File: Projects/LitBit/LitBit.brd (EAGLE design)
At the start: 160 x 100 mm, 1 part

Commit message: almost milestoneeeE??
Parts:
- removed U$1: ATMEGA32U4-AU, adafruit:TQFP44
- added C1, C18, C19: 10uF, SCADA_CUSTOM_LIBRARY:0603-POLAR
- added C10, C11, C15: 100nF, SCADA_CUSTOM_LIBRARY:0603-CUSTOM
- added C12, C13, C16, C17, C7, C8: 12p, SCADA_CUSTOM_LIBRARY:0603-CUSTOM
- added C14, C26: 1uF, SCADA_CUSTOM_LIBRARY:0603-CUSTOM
- added C2, C25, C3: 4.7uF, SCADA_CUSTOM_LIBRARY:0603-CUSTOM
- added C20: 1 nF, SCADA_CUSTOM_LIBRARY:0603-CUSTOM
- added C21: 1.2 pF, SCADA_CUSTOM_LIBRARY:0603-CUSTOM
- added C22: 1.5 pF, SCADA_CUSTOM_LIBRARY:0603-CUSTOM
- added C23: 1.8 pF, SCADA_CUSTOM_LIBRARY:0603-CUSTOM
- added C24: 2.2 nF, SCADA_CUSTOM_LIBRARY:0603-CUSTOM
- added C27, C4, C5, C6: 100n, SCADA_CUSTOM_LIBRARY:0603-CUSTOM
- added C28, C29: 22p, SCADA_CUSTOM_LIBRARY:0603-CUSTOM
- added C9: 33nF, SCADA_CUSTOM_LIBRARY:0603-CUSTOM
- added D1: Green, Wurth_Elektronik_Optoelectronics_rev18a:WL-SMCW_0603
- added FB1, FB2: (no value), SCADA_CUSTOM_LIBRARY:0603-CUSTOM
- added ISP1: AVRISP-6, adafruit:AVRISP
- added JMP1: 0R-JUMPA, SCADA_CUSTOM_LIBRARY:AOR-JMP-0603
- added JP1, JP10, JP2, JP3, JP4, JP5, JP6, JP7, JP9: (no value), microbuilder:JUMPER2
- added JP11: BLE_SPI, jumper:JP3Q
- added JP12: Display, adafruit:1X06
- added JP8: I2c, pinhead:1X02
- added L1: 15 nH, SCADA_CUSTOM_LIBRARY:0603-CUSTOM
- added L2: 10 uH, SCADA_CUSTOM_LIBRARY:0805-CUSTOM
- added L3: 5.6 nH, SCADA_CUSTOM_LIBRARY:0603-CUSTOM
- added L4: 8.2 nH, SCADA_CUSTOM_LIBRARY:0603-CUSTOM
- added L5: 3.9 nH, SCADA_CUSTOM_LIBRARY:0603-CUSTOM
- added R1: 22k, SCADA_CUSTOM_LIBRARY:0603-CUSTOM
- added R2, R7: 0R, SCADA_CUSTOM_LIBRARY:0603-CUSTOM
- added R3: 47k, SCADA_CUSTOM_LIBRARY:0603-CUSTOM
- added R4: 330, SCADA_CUSTOM_LIBRARY:0603-CUSTOM
- added R5, R6, R8: 10k, SCADA_CUSTOM_LIBRARY:0603-CUSTOM
- added TP1: TEST_POINT_40MIL_DIA, SCADA_CUSTOM_LIBRARY:TEST_POINT_40MIL_DIA
- added U$28: (no value), microbuilder:ANT_PCB_2.4GHZ_NRF8001_1.6MM_1OZ
- added U1: 24FC1025, SCADA_CUSTOM_LIBRARY:8-SOIC_HAND_SOLDER
- added U2: MCP7490N, SCADA_CUSTOM_LIBRARY:8-SOIC_HAND_SOLDER
- added U3: ADXL345, SCADA_CUSTOM_LIBRARY:LGA-14
- added U4: ATMEGA32U4-AU, SCADA_CUSTOM_LIBRARY:TQFP44
- added U5: S-1335J33-M5T1U3, SCADA_CUSTOM_LIBRARY:SOT23-5_HAND_SOLDER
- added U6: nRF8001, microbuilder:QFN32_5MM
- added U7: MCP73831, SCADA_CUSTOM_LIBRARY:SOT23-5_HAND_SOLDER
- added USB1: ZX62-B-5PA, Seeed-Connector:MICRO-USB5+6P-SMD-0.65-AB
- added Y1: 16.0000 MHz, SCADA_CUSTOM_LIBRARY:4-SMD
- added Y2, Y3: 32.7680 kHz, SCADA_CUSTOM_LIBRARY:4-SOJ
- added Y4: 8.0000 MHz, adafruit:HC49UP
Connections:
- new net 3.3V: C19.1, FB1.1, ISP1.2, JMP1.3, JP2.2, JP3.2, JP5.2, JP9.2, R5.2, R6.2, R7.1, U5.5
- new net ACTIVE: U6.6
- new net AGND: R2.1, U3.2, U3.4, U3.5
- new net AVCC: JP10.2, JP7.2, R7.2
- new net D+: U4.4, USB1.3
- new net D-: U4.3, USB1.2
- new net MFP: R8.1, U2.7
- new net MISO: ISP1.1, JP11.5
- new net MISO_3V3: JP11.6, U6.14
- new net MOSI: ISP1.4, JP11.3, U4.10
- new net MOSI_3V3: JP11.4, U6.13
- new net N$1: C7.2, U2.1, Y3.P4
- new net N$10: L1.1, L2.2
- new net N$11: L2.1, U6.32
- new net N$12: C16.1, U6.28, Y1.P3
- new net N$13: JMP1.2, U5.4
- new net N$14: C18.1, JP1.1, U5.1, U5.3
- new net N$15: C4.1, JP2.1, R8.2, U2.8
- new net N$16: C3.1, JP4.1, U7.3
- new net N$17: C26.1, C5.1, JP3.1, U1.3, U1.8
- new net N$18: C17.1, U6.27, Y1.P1
- new net N$19: C23.2, L5.2
- new net N$2: C8.2, U2.2, Y3.P1
- new net N$20: L4.2, L5.1, U6.22
- new net N$21: L3.1, L4.1, U6.21
- new net N$22: R1.1, U6.25
- new net N$23: C24.1, L3.2, U6.20
- new net N$24: C21.1, C22.1, C23.1, U$28.FEED
- new net N$25: D1.1, R4.2
- new net N$26: R3.2, U7.5
- new net N$27: R4.1, U7.1
- new net N$28: C25.1, JP9.1, U4.14, U4.34
- new net N$29: C28.2, U4.16, Y4.1
- new net N$3: C10.1, U6.2
- new net N$30: C29.2, U4.17, Y4.2
- new net N$32: FB2.2, JP10.1
- new net N$33: C27.1, FB2.1, U4.24, U4.44
- new net N$34: TP1.TP$1, U4.42
- new net N$4: C9.1, U6.3
- new net N$5: C12.2, U6.4, Y2.P4
- new net N$6: C13.2, U6.5, Y2.P1
- new net N$7: C2.1, D1.2, JP6.1, U7.4
- new net N$8: C1.1, C15.1, JP5.1, U6.1, U6.9
- new net N$9: C6.2, JP7.1, U3.6
- new net RDYN: U6.16
- new net REQN_3V3: U6.12
- new net RST: ISP1.5, U4.13
- new net RST_NRF: U6.19
- new net SCK: ISP1.3, JP11.1, U4.9
- new net SCK_3V3: JP11.2, U6.11
- new net SCL: JP8.2, R5.1, U1.6, U2.6, U3.14, U4.18
- new net SDA: JP8.1, R6.1, U1.5, U2.5, U3.13, U4.19
- new net SHIELD: USB1.5, USB1.P1, USB1.P2, USB1.P3, USB1.P4, USB1.P5, USB1.P6
- new net VDDA: C11.1, C14.1, C20.1, FB1.2, L1.2, U6.24, U6.26, U6.29
- new net V_BATT: JP1.2, JP4.2
- new net V_USB: JP6.2, U4.7, USB1.1
- net GND: now also C1.2, C10.2, C11.2, C12.1, C13.1, C14.2, C15.2, C16.2, C17.2, C18.2, C19.2, C2.2, C20.2, C21.2, C22.2, C24.2, C25.2, C26.2, C27.2, C28.1, C29.1, C3.2, C4.2, C5.2, C6.1, C7.1, C8.1, C9.2, ISP1.6, JMP1.1, R1.2, R2.2, R3.1, U1.1, U1.2, U1.4, U1.7, U2.3, U2.4, U4.15, U4.23, U4.35, U4.43, U4.5, U5.2, U6.17, U6.18, U6.23, U6.30, U6.31, U6.33, U6.8, U7.2; no longer U$1.15, U$1.23, U$1.35, U$1.43
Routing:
- added copper zone on layer 1, net GND

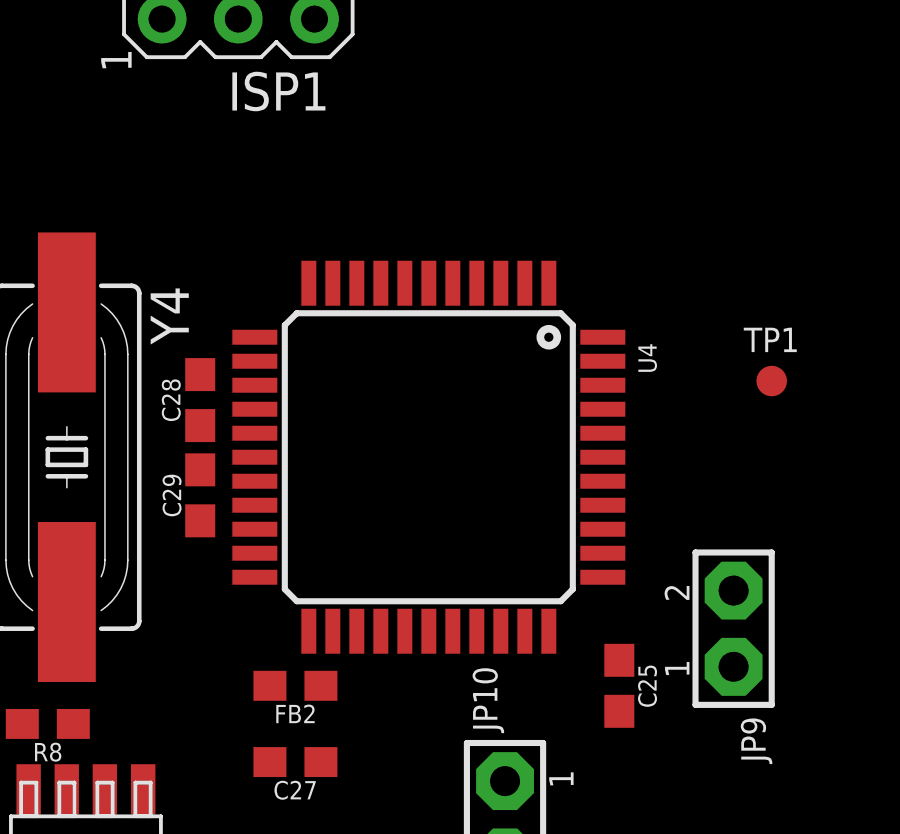
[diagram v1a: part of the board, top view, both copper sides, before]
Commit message: Change processor package to VQFN to save space.
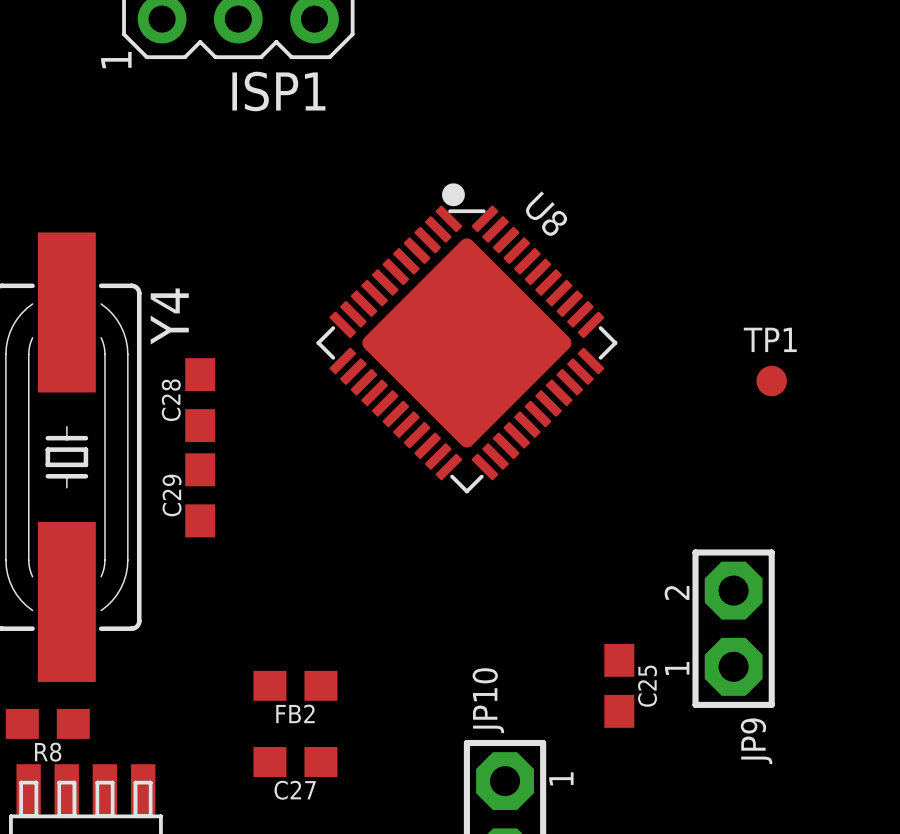
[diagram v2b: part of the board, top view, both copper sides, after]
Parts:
- removed U4: ATMEGA32U4-AU, SCADA_CUSTOM_LIBRARY:TQFP44
- added U8: ATMEGA32U4-MUR-QFN44, Seeed-IC:QFN44G-0.5-7X7MM
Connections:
- net D+: now also U8.4; no longer U4.4
- net D-: now also U8.3; no longer U4.3
- net GND: now also U8.15, U8.23, U8.35, U8.43, U8.5, U8.TAB; no longer U4.15, U4.23, U4.35, U4.43, U4.5
- net MOSI: no longer U4.10
- net N$28: now also U8.14, U8.34; no longer U4.14, U4.34
- net N$29: now also U8.16; no longer U4.16
- net N$30: now also U8.17; no longer U4.17
- net N$33: now also U8.24, U8.44; no longer U4.24, U4.44
- net N$34: no longer U4.42
- net RST: now also U8.13; no longer U4.13
- net SCK: no longer U4.9
- net SCL: no longer U4.18
- net SDA: no longer U4.19
- net V_USB: now also U8.7; no longer U4.7
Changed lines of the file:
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@@
 <elements>
 <element name="U1" library="SCADA_CUSTOM_LIBRARY" package="8-SOIC_HAND_SOLDER" value="24FC1025" x="84.455" y="8.255" rot="R90"/>
-<element name="U4" library="SCADA_CUSTOM_LIBRARY" package="TQFP44" value="ATMEGA32U4-AU" x="69.215" y="29.21" rot="R270"/>
 <element name="U2" library="SCADA_CUSTOM_LIBRARY" package="8-SOIC_HAND_SOLDER" value="MCP7490N" x="57.785" y="15.24" rot="R90"/>
 <element name="C1" library="SCADA_CUSTOM_LIBRARY" package="0603-POLAR" value="10uF" x="31.75" y="74.295" rot="R180"/>
@@
 <element name="JP12" library="adafruit" library_urn="urn:adsk.eagle:library:420" package="1X06" value="Display" x="9.525" y="22.86" rot="R90"/>
 <element name="U$28" library="microbuilder" package="ANT_PCB_2.4GHZ_NRF8001_1.6MM_1OZ" value="" x="12.065" y="52.705"/>
+<element name="U8" library="Seeed-IC" library_urn="urn:adsk.eagle:library:470" package="QFN44G-0.5-7X7MM" package3d_urn="urn:adsk.eagle:package:32646/1" value="ATMEGA32U4-MUR-QFN44" x="70.485" y="33.02" rot="R315">
+<attribute name="MPN" value="ATMEGA32U4-MUR" x="70.485" y="33.02" size="1.778" layer="27" rot="R315" display="off"/>
+</element>
 </elements>
 <signals>
 <signal name="GND">
-<contactref element="U4" pad="15"/>
-<contactref element="U4" pad="23"/>
-<contactref element="U4" pad="35"/>
-<contactref element="U4" pad="43"/>
 <contactref element="U2" pad="4"/>
 <contactref element="U1" pad="4"/>
@@
 <contactref element="U1" pad="7"/>
 <contactref element="C27" pad="2"/>
-<contactref element="U4" pad="5"/>
 <contactref element="C29" pad="1"/>
 <contactref element="C28" pad="1"/>
 <contactref element="ISP1" pad="6"/>
-<wire x1="24.88" y1="57.825" x2="24.13" y2="60.325" width="0" layer="19" extent="1-1"/>
+<contactref element="U8" pad="5"/>
+<contactref element="U8" pad="43"/>
+<contactref element="U8" pad="35"/>
+<contactref element="U8" pad="23"/>
+<contactref element="U8" pad="15"/>
+<contactref element="U8" pad="TAB"/>
+<wire x1="68.46974375" y1="35.742359375" x2="70.485" y2="33.02" width="0" layer="19" extent="1-1"/>
+<wire x1="24.13" y1="60.325" x2="24.88" y2="57.825" width="0" layer="19" extent="1-1"/>
 </signal>
 <signal name="3.3V">
@@
 <signal name="V_USB">
 <contactref element="JP6" pad="2"/>
-<contactref element="U4" pad="7"/>
 <contactref element="USB1" pad="1"/>
+<contactref element="U8" pad="7"/>
 <wire x1="59.72" y1="64.435" x2="62.23" y2="62.23" width="0" layer="19" extent="1-1"/>
-<wire x1="68.415" y1="35.01" x2="62.23" y2="62.23" width="0" layer="19" extent="1-1"/>
+<wire x1="67.7626375" y1="35.035253125" x2="62.23" y2="62.23" width="0" layer="19" extent="1-1"/>
 </signal>
 <signal name="N$9">
@@
 <contactref element="JP8" pad="1"/>
 <contactref element="R6" pad="1"/>
-<contactref element="U4" pad="19"/>
 <wire x1="86.365" y1="11.155" x2="94.71" y2="18.5469" width="0" layer="19" extent="1-1"/>
 <wire x1="59.695" y1="18.14" x2="86.365" y2="11.155" width="0" layer="19" extent="1-1"/>
-<wire x1="63.415" y1="27.61" x2="59.695" y2="18.14" width="0" layer="19" extent="1-1"/>
-<wire x1="46.99" y1="30.48" x2="63.415" y2="27.61" width="0" layer="19" extent="1-1"/>
+<wire x1="46.99" y1="30.48" x2="59.695" y2="18.14" width="0" layer="19" extent="1-1"/>
 <wire x1="44.665" y1="30.48" x2="46.99" y2="30.48" width="0" layer="19" extent="1-1"/>
 </signal>
@@
 <contactref element="JP8" pad="2"/>
 <contactref element="R5" pad="1"/>
-<contactref element="U4" pad="18"/>
 <wire x1="85.085" y1="11.155" x2="94.81" y2="19.685" width="0" layer="19" extent="1-1"/>
 <wire x1="58.415" y1="18.14" x2="85.085" y2="11.155" width="0" layer="19" extent="1-1"/>
-<wire x1="63.415" y1="28.41" x2="58.415" y2="18.14" width="0" layer="19" extent="1-1"/>
 <wire x1="46.99" y1="27.94" x2="58.415" y2="18.14" width="0" layer="19" extent="1-1"/>
 <wire x1="44.665" y1="27.94" x2="46.99" y2="27.94" width="0" layer="19" extent="1-1"/>
@@
 <contactref element="JP9" pad="1"/>
 <contactref element="C25" pad="1"/>
-<contactref element="U4" pad="14"/>
-<contactref element="U4" pad="34"/>
-<wire x1="75.565" y1="22.44" x2="79.375" y2="22.225" width="0" layer="19" extent="1-1"/>
-<wire x1="75.015" y1="25.21" x2="75.565" y2="22.44" width="0" layer="19" extent="1-1"/>
-<wire x1="63.415" y1="31.61" x2="75.015" y2="25.21" width="0" layer="19" extent="1-1"/>
+<contactref element="U8" pad="14"/>
+<contactref element="U8" pad="34"/>
+<wire x1="67.05553125" y1="31.71185" x2="74.621571875" y2="33.621040625" width="0" layer="19" extent="1-1"/>
+<wire x1="75.565" y1="22.44" x2="74.621571875" y2="33.621040625" width="0" layer="19" extent="1-1"/>
+<wire x1="79.375" y1="22.225" x2="75.565" y2="22.44" width="0" layer="19" extent="1-1"/>
 </signal>
 <signal name="MFP">
@@
 </signal>
 <signal name="N$33">
-<contactref element="U4" pad="24"/>
 <contactref element="C27" pad="1"/>
 <contactref element="FB2" pad="1"/>
-<contactref element="U4" pad="44"/>
-<wire x1="66.015" y1="23.41" x2="75.015" y2="33.21" width="0" layer="19" extent="1-1"/>
-<wire x1="65.62" y1="21.59" x2="66.015" y2="23.41" width="0" layer="19" extent="1-1"/>
+<contactref element="U8" pad="24"/>
+<contactref element="U8" pad="44"/>
+<wire x1="71.43959375" y1="29.236978125" x2="71.086040625" y2="37.156571875" width="0" layer="19" extent="1-1"/>
+<wire x1="65.62" y1="21.59" x2="71.43959375" y2="29.236978125" width="0" layer="19" extent="1-1"/>
 <wire x1="65.62" y1="19.05" x2="65.62" y2="21.59" width="0" layer="19" extent="1-1"/>
 </signal>
 <signal name="N$34">
-<contactref element="U4" pad="42"/>
 <contactref element="TP1" pad="TP$1"/>
-<wire x1="75.015" y1="31.61" x2="80.645" y2="31.75" width="0" layer="19" extent="1-1"/>
 </signal>
 <signal name="N$29">
-<contactref element="U4" pad="16"/>
 <contactref element="Y4" pad="1"/>
 <contactref element="C28" pad="2"/>
-<wire x1="61.595" y1="30.265" x2="63.415" y2="30.01" width="0" layer="19" extent="1-1"/>
+<contactref element="U8" pad="16"/>
+<wire x1="61.595" y1="30.265" x2="67.7626375" y2="31.00474375" width="0" layer="19" extent="1-1"/>
 <wire x1="57.15" y1="34.036" x2="61.595" y2="30.265" width="0" layer="19" extent="1-1"/>
 </signal>
 <signal name="N$30">
-<contactref element="U4" pad="17"/>
 <contactref element="Y4" pad="2"/>
 <contactref element="C29" pad="2"/>
-<wire x1="61.595" y1="28.79" x2="63.415" y2="29.21" width="0" layer="19" extent="1-1"/>
+<contactref element="U8" pad="17"/>
+<wire x1="61.595" y1="28.79" x2="68.116190625" y2="30.651190625" width="0" layer="19" extent="1-1"/>
 <wire x1="57.15" y1="24.384" x2="61.595" y2="28.79" width="0" layer="19" extent="1-1"/>
 </signal>
@@
 <signal name="D+">
 <contactref element="USB1" pad="3"/>
-<contactref element="U4" pad="4"/>
-<wire x1="70.815" y1="35.01" x2="58.42" y2="64.435" width="0" layer="19" extent="1-1"/>
+<contactref element="U8" pad="4"/>
+<wire x1="68.823296875" y1="36.0959125" x2="58.42" y2="64.435" width="0" layer="19" extent="1-1"/>
 </signal>
 <signal name="D-">
 <contactref element="USB1" pad="2"/>
-<contactref element="U4" pad="3"/>
-<wire x1="71.615" y1="35.01" x2="59.07" y2="64.435" width="0" layer="19" extent="1-1"/>
+<contactref element="U8" pad="3"/>
+<wire x1="69.17685" y1="36.449465625" x2="59.07" y2="64.435" width="0" layer="19" extent="1-1"/>
 </signal>
 <signal name="MISO">
@@
 </signal>
 <signal name="MOSI">
-<contactref element="U4" pad="10"/>
 <contactref element="ISP1" pad="4"/>
 <contactref element="JP11" pad="3"/>
-<wire x1="66.015" y1="35.01" x2="62.865" y2="46.355" width="0" layer="19" extent="1-1"/>
 <wire x1="23.495" y1="71.755" x2="62.865" y2="46.355" width="0" layer="19" extent="1-1"/>
 </signal>
 <signal name="SCK">
-<contactref element="U4" pad="9"/>
 <contactref element="ISP1" pad="3"/>
 <contactref element="JP11" pad="1"/>
-<wire x1="66.815" y1="35.01" x2="62.865" y2="43.815" width="0" layer="19" extent="1-1"/>
 <wire x1="26.035" y1="71.755" x2="62.865" y2="43.815" width="0" layer="19" extent="1-1"/>
 </signal>
 <signal name="RST">
-<contactref element="U4" pad="13"/>
 <contactref element="ISP1" pad="5"/>
-<wire x1="63.415" y1="32.41" x2="65.405" y2="43.815" width="0" layer="19" extent="1-1"/>
+<contactref element="U8" pad="13"/>
+<wire x1="66.701978125" y1="32.065403125" x2="65.405" y2="43.815" width="0" layer="19" extent="1-1"/>
 </signal>
 </signals>
